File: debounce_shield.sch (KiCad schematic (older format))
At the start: 51 parts, among them J1 Conn_01x06, J2 RPi_GPIO, J3 Conn_01x06, J4 Conn_01x06, K1 CONN_3, P2 CONN_2, U1 74LVT04, U2 CAT24C32, U3 LTV-824, U4 LTV-824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

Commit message: Update schematic and PCB to revision 1.2
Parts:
- removed D7: DIODE, Diode_SMD:D_0805_2012Metric_Pad1.15x1.40mm_HandSolder, symbol debounce_shield-rescue:DIODE-debounce_shield-rescue
- removed PS1: REE-0505S, SamacSys_Parts:REE0505S, symbol debounce_shield-rescue:REE-0505S-SamacSys_Parts
- removed R1, R2, R3: YC164-JR-0710KL, SamacSys_Parts:YC164, symbol debounce_shield-rescue:YC164-JR-0710KL-SamacSys_Parts
- added PS1: RFMM-0505S, RFMM-0505S:RFMM0505S, symbol RFMM-0505S:RFMM-0505S
- added Q1: DMMT5401-7, DMMT5401-7:SOT95P275X110-6N, symbol DMMT5401-7:DMMT5401-7
- added Q2: DMG2305UX-7, DMG2305UX-7:SOT96P240X100-3N, symbol DMG2305UX-7:DMG2305UX-7
- added R1: 10k 1%, Resistor_SMD:R_0603_1608Metric, symbol Device:R_Small
- added R2: 47k 1%, Resistor_SMD:R_0603_1608Metric, symbol Device:R_Small
- added RN1, RN2: YC164-JR-07100RL, YC164-JR-07100RL:YC164JR07220RL, symbol YC164-JR-07100RL:YC164-JR-07100RL
- added RN3: YC164-JR-07100RL, YC164JR07220RL, symbol YC164-JR-07100RL:YC164-JR-07100RL
- C1, C2, C3, C4, C5, C6, C7, C8: footprint Capacitor_SMD:C_0805_2012Metric_Pad1.15x1.40mm_HandSolder -> Capacitor_SMD:C_0603_1608Metric
- R19, R20, R21: footprint Resistor_SMD:R_0805_2012Metric_Pad1.15x1.40mm_HandSolder -> Resistor_SMD:R_0603_1608Metric
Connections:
- wire segments 295 -> 319
- no-connect marks 22 -> 21
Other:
- moved on the sheet: P2

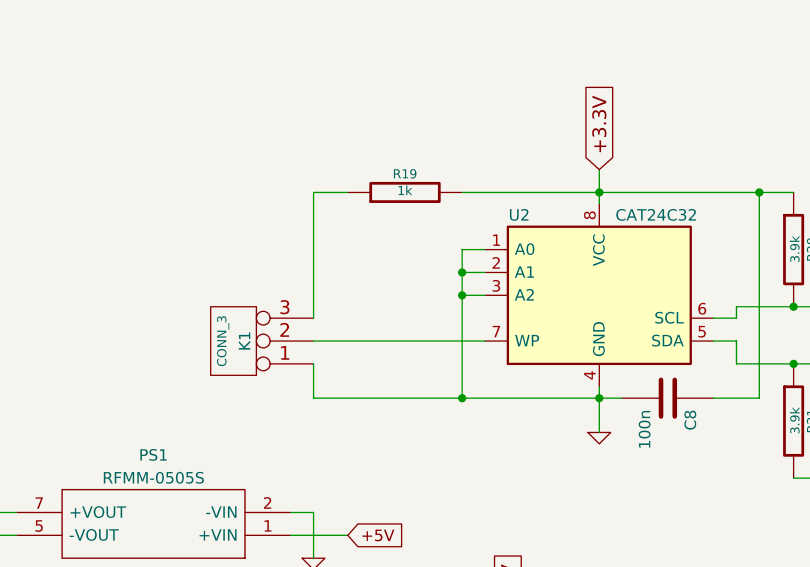
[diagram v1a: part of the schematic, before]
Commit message: Reduce WP header to two pins. Clean-up PCB layout. Re-add art.
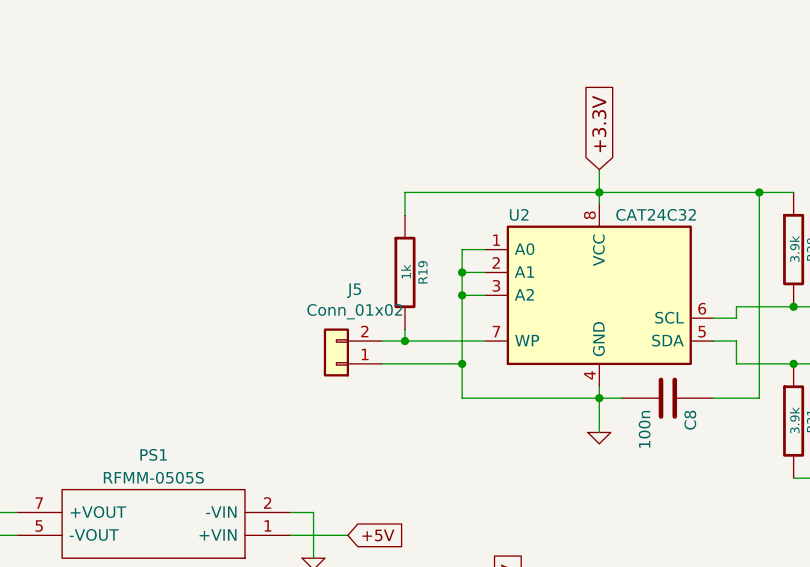
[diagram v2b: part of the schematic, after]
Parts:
- removed K1: CONN_3, Connector_PinHeader_2.54mm:PinHeader_1x03_P2.54mm_Vertical, symbol debounce_shield-rescue:CONN_3-debounce_shield-rescue
- added J5: Conn_01x02, Connector_PinHeader_2.54mm:PinHeader_1x02_P2.54mm_Vertical, symbol Connector_Generic:Conn_01x02
- RN3: footprint YC164JR07220RL -> YC164-JR-07100RL:YC164JR07220RL
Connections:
- net GND: now also J5.1 (Pin_1)
- net VDD: now also R19.1; no longer R19.2
- net at U2.7 (WP): now also R19.2, J5.2 (Pin_2)
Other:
- moved on the sheet: R19
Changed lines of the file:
@@
 L debounce_shield-rescue:R-debounce_shield-rescue R19
 U 1 1 5AAC3346
-P 4400 1500
-F 0 "R19" V 4480 1500 40  0000 C CNN
-F 1 "1k" V 4407 1501 40  0000 C CNN
-F 2 "Resistor_SMD:R_0603_1608Metric" V 4330 1500 30  0001 C CNN
-F 3 "" H 4400 1500 30  0000 C CNN
-	1    4400 1500
-	0    -1   -1   0
+P 4400 1850
+F 0 "R19" V 4480 1850 40  0000 C CNN
+F 1 "1k" V 4407 1851 40  0000 C CNN
+F 2 "Resistor_SMD:R_0603_1608Metric" V 4330 1850 30  0001 C CNN
+F 3 "" H 4400 1850 30  0000 C CNN
+	1    4400 1850
+	1    0    0    -1
 $EndComp
 Wire Wire Line
@@
 Wire Wire Line
 	5850 2150 5750 2150
-Wire Wire Line
-	4650 1500 5250 1500
 Connection ~ 5250 1500
 Wire Wire Line
-	4000 2150 4750 2150
-Wire Wire Line
 	4750 1750 4650 1750
 Wire Wire Line
 	4650 1750 4650 1850
-Wire Wire Line
-	4000 2400 4650 2400
 Connection ~ 5250 2400
 Wire Wire Line
@@
 	4750 1850 4650 1850
 Connection ~ 4650 1850
-$Comp
-L debounce_shield-rescue:CONN_3-debounce_shield-rescue K1
-U 1 1 5AAC3F88
-P 3650 2150
-F 0 "K1" V 3600 2150 50  0000 C CNN
-F 1 "CONN_3" V 3700 2150 40  0000 C CNN
-F 2 "Connector_PinHeader_2.54mm:PinHeader_1x03_P2.54mm_Vertical" H 3650 2150 60  0001 C CNN
-F 3 "" H 3650 2150 60  0001 C CNN
-	1    3650 2150
-	-1   0    0    1
-$EndComp
-Wire Wire Line
-	4000 2050 4000 1500
-Wire Wire Line
-	4000 1500 4150 1500
-Wire Wire Line
-	4000 2250 4000 2400
-Connection ~ 4650 2400
 Wire Wire Line
 	7700 1200 7850 1200
@@
 	5250 2400 5250 2350
 Wire Wire Line
-	4650 1950 4650 2400
+	4650 1950 4650 2250
 Wire Wire Line
 	4650 1850 4650 1950
@@
 F 0 "RN3" H 4350 5965 50  0000 C CNN
 F 1 "YC164-JR-07100RL" H 4350 5874 50  0000 C CNN
-F 2 "YC164JR07220RL" H 4600 5800 50  0001 L CNN
+F 2 "YC164-JR-07100RL:YC164JR07220RL" H 4600 5800 50  0001 L CNN
 F 3 "http://www.yageo.com/documents/recent/PYu-YC_TC164_51_RoHS_L_(3).pdf" H 4600 5700 50  0001 L CNN
 F 4 "YAGEO - YC164-JR-07100RL - RESISTOR ARRAY, ARV241 1206 100R" H 4600 5600 50  0001 L CNN "Description"
@@
 	7450 3950 7450 3150
 NoConn ~ 7600 3150
+$Comp
+L Connector_Generic:Conn_01x02 J5
+U 1 1 5D4A9ED5
+P 4100 2250
+F 0 "J5" H 4018 1925 50  0000 C CNN
+F 1 "Conn_01x02" H 4018 2016 50  0000 C CNN
+F 2 "Connector_PinHeader_2.54mm:PinHeader_1x02_P2.54mm_Vertical" H 4100 2250 50  0001 C CNN
+F 3 "~" H 4100 2250 50  0001 C CNN
+	1    4100 2250
+	-1   0    0    1
+$EndComp
+Wire Wire Line
+	4400 1500 4400 1600
+Wire Wire Line
+	4400 1500 5250 1500
+Wire Wire Line
+	4400 2100 4400 2150
+Connection ~ 4400 2150
+Wire Wire Line
+	4400 2150 4750 2150
+Wire Wire Line
+	4300 2150 4400 2150
+Wire Wire Line
+	4300 2250 4650 2250
+Connection ~ 4650 2250
+Wire Wire Line
+	4650 2250 4650 2400
 $EndSCHEMATC

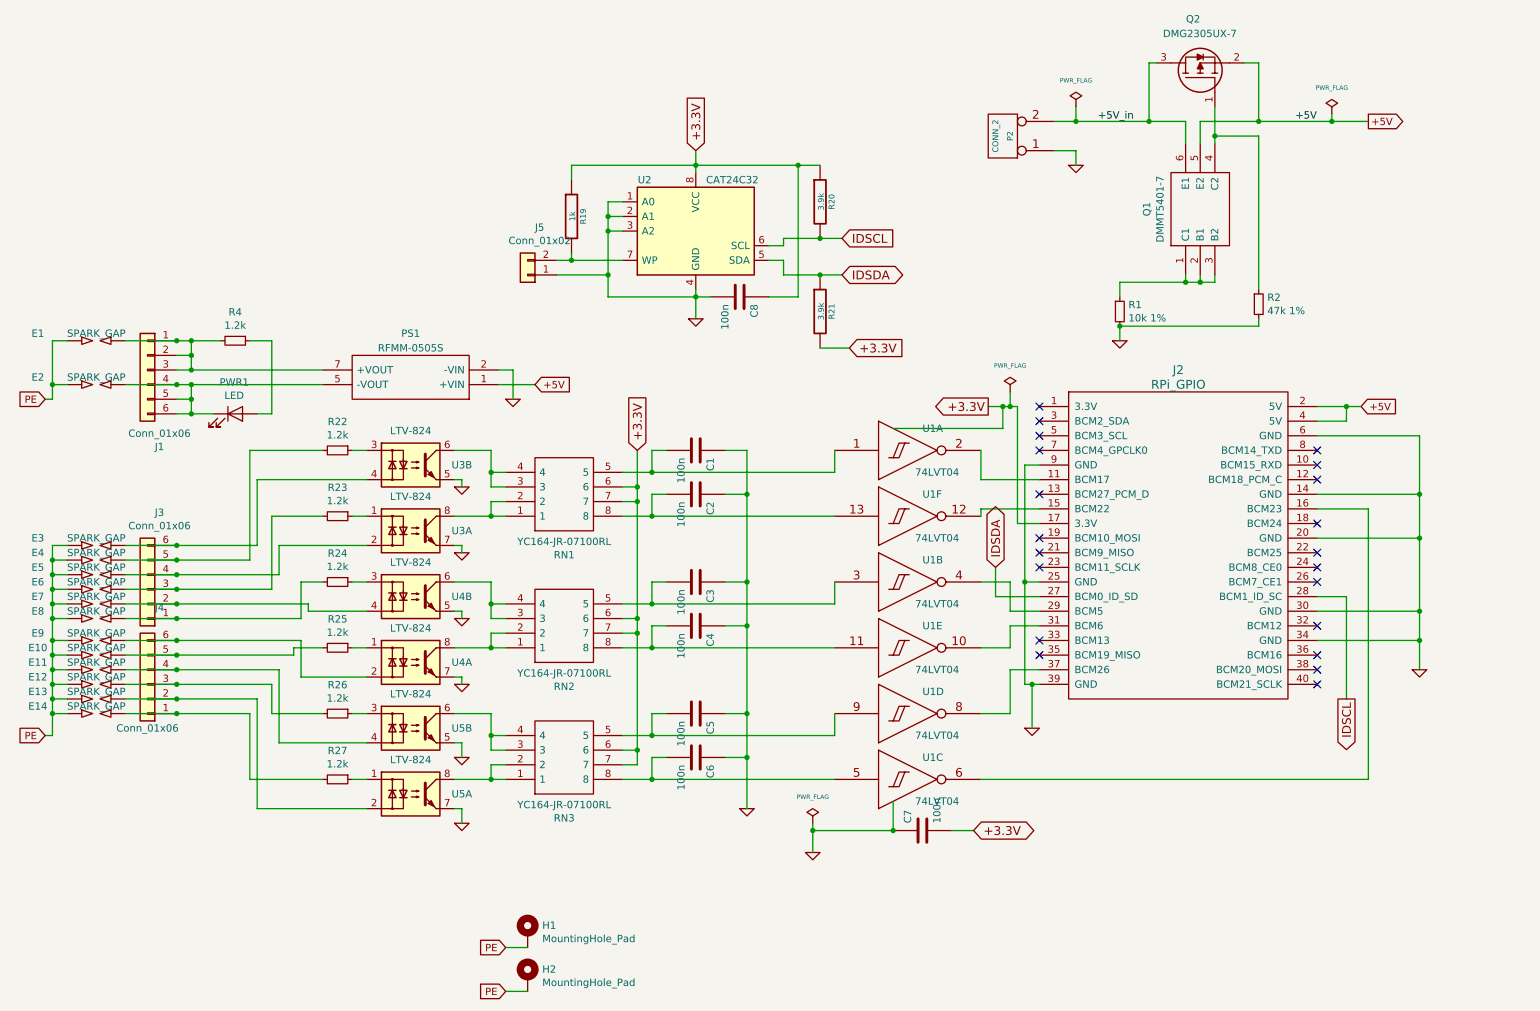
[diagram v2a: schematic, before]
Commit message: Update README. Add GPIO graphic.
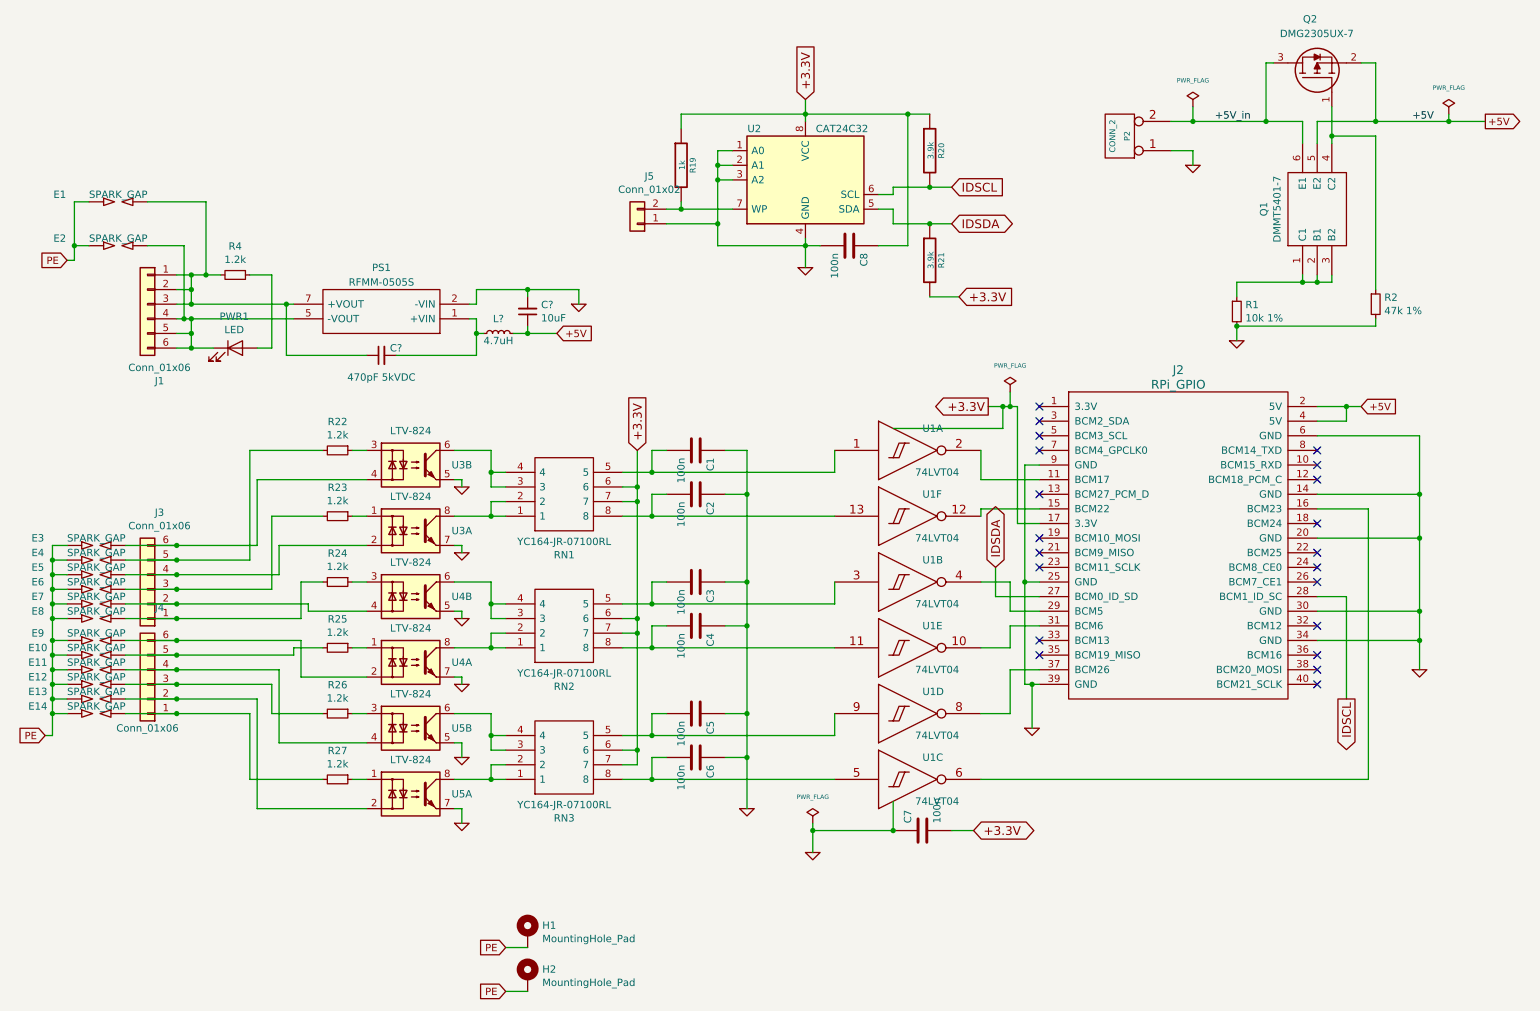
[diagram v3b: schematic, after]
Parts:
- added C?: 10uF, symbol Device:C_Small
- added C?: 470pF 5kVDC, symbol Device:C_Small
- added L?: 4.7uH, symbol Device:L_Small
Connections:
- net +5V: now also C?.1, L?.2; no longer PS1.1 (+VIN)
- net GND: now also C?.2
- net at E1.2, J1.1 (Pin_1), J1.2 (Pin_2)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: now also C?.1
- new net: C?.2, L?.1, PS1.1 (+VIN)
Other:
- moved on the sheet: C8, E1, E2, J1, J5, P2, PS1, PWR1, Q1, Q2, R1, R19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

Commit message: Replace RFMM DC-DC with RKZE. Add EMC components.
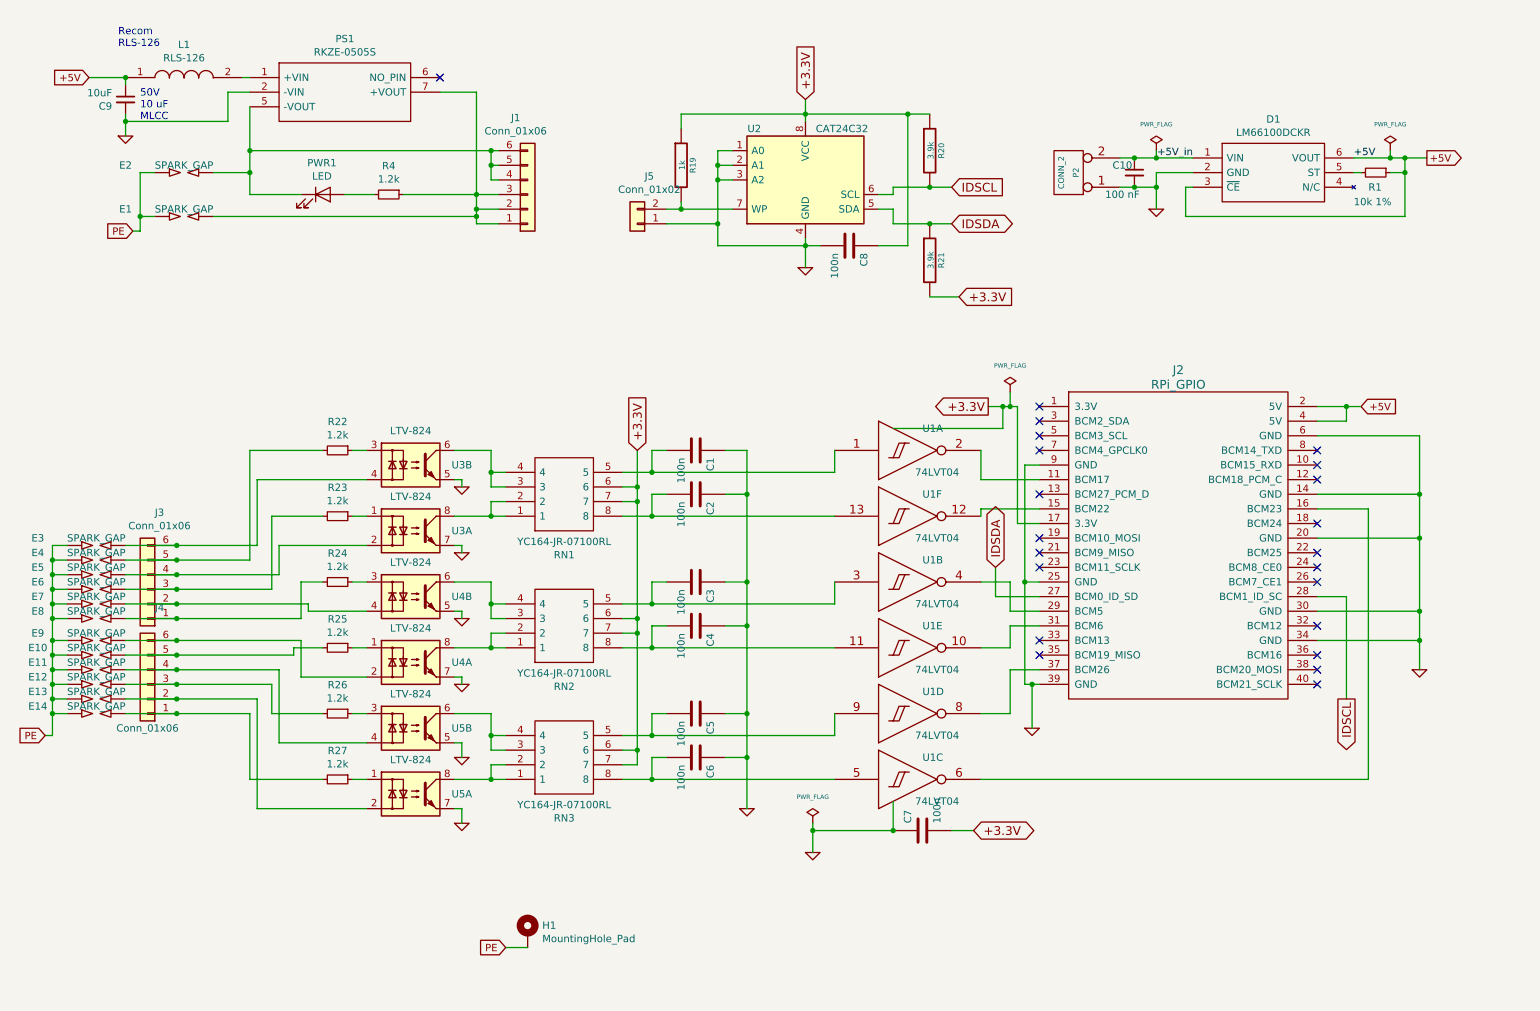
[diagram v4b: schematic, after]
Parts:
- removed C?: 470pF 5kVDC, symbol Device:C_Small
- removed H2: MountingHole_Pad, MountingHole:MountingHole_3.5mm_Pad, symbol Mechanical:MountingHole_Pad
- removed L?: 4.7uH, symbol Device:L_Small
- removed PS1: RFMM-0505S, RFMM-0505S:RFMM0505S, symbol RFMM-0505S:RFMM-0505S
- removed Q1: DMMT5401-7, DMMT5401-7:SOT95P275X110-6N, symbol DMMT5401-7:DMMT5401-7
- removed Q2: DMG2305UX-7, DMG2305UX-7:SOT96P240X100-3N, symbol DMG2305UX-7:DMG2305UX-7
- removed R2: 47k 1%, Resistor_SMD:R_0603_1608Metric, symbol Device:R_Small
- added C10: 100 nF, Capacitor_SMD:C_0603_1608Metric, symbol Device:C_Small
- added D1: LM66100DCKR, LM66100DCKR:SOP65P210X110-6N, symbol LM66100DCKR:LM66100DCKR
- added L1: RLS-126, RLS-126:RLS126, symbol RLS-126:RLS-126
- added PS1: RKZE-0505S, RKZE-0505S:RKZE0512SHP, symbol RKZE-0505S:RKZE-0505S
- C9: renamed from C?; footprint (none) -> Capacitor_SMD:C_1206_3216Metric
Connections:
- net +5V: now also R1.1, D1.3 (~CE), D1.6 (VOUT), L1.1
- net +5V_in: now also C10.1, D1.1 (VIN)
- net GND: now also C10.2, D1.2 (GND), PS1.2 (-VIN); no longer R1.2
- net at E1.2, J1.1 (Pin_1), J1.2 (Pin_2)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: now also R4.1, PS1.7 (+VOUT); no longer R4.2
- net at E2.2, J1.4 (Pin_4), J1.5 (Pin_5)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: now also PS1.5 (-VOUT)
- net at PWR1.2 (A): now also R4.2; no longer R4.1
- new net: D1.5 (ST), R1.2
- new net: L1.2, PS1.1 (+VIN)
- no-connect marks 21 -> 22
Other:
- note added: "50V\n10 uF\nMLCC"
- note added: "Recom\nRLS-126"
- moved on the sheet: C9, E1, E2, J1, P2, PWR1, R1, R4

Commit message: Update schematic & PCB with new terminal connectors.
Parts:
- C1, C10, C2, C3, C4, C5, C6, C7, C8: Manufacturer_Name (none) -> Wurth Elektronik; Manufacturer_Part_Number (none) -> 885012206071; Mouser Part Number (none) -> 710-885012206071
- C9: Manufacturer_Name (none) -> Taiyo Yuden; Manufacturer_Part_Number (none) -> UMK316BBJ106ML-T; Mouser Part Number (none) -> 963-UMK316BBJ106ML-T
- J1, J3, J4: footprint SamacSys_Parts:GSL002C25006P -> GSL002C-2.50-06P:GSL002C25006P
- J2: Manufacturer_Name (none) -> Adafruit; Manufacturer_Part_Number (none) -> 1979; Mouser Part Number (none) -> 485-1979
- PWR1: Mouser Part Number (none) -> 604-AP2012HD
- R22, R23, R24, R25, R26, R27, R4: Mouser Part Number (none) -> 71-CRCW12061K20JNEB
- U1: value 74LVT04 -> 74LV14D; Mouser Part Number (none) -> 771-LV14D112
- U2: Mouser Part Number (none) -> 698-CAT24C32WI-GT3
- U3, U4, U5: Mouser Part Number (none) -> 859-LTV-824
